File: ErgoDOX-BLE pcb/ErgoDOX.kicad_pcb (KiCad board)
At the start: 2 copper layers, 182.8 x 158.9 mm, 118 parts, among them J1 Conn_01x04, J2 Conn_01x02_Female, J3 Conn_01x02_Female, J4 Conn_01x02, J5 Conn_01x02, J6 6PIN, P1 USB_C_Plug_USB2.0, Q1 Q_NPN_BCE, SW0:10 SW0:3, SW0:11 SW0:2, SW0:12 SW0:1, SW0:7 SW0:6, SW0:8 SW0:5, SW0:9 SW0:4, SW1:10 SW1:3, SW1:11 SW1:2, SW1:12 SW1:1, SW1:13 SW1:0, SW1:9 SW1:4, SW2:10 SW2:3, SW2:11 SW2:2, SW2:12 SW2:1, SW2:13 SW2:0, SW2:7 SW2:6, SW2:8 SW2:5, SW2:9 SW2:4, SW3:10 SW3:3, SW3:11 SW3:2, SW3:12 SW3:1, SW3:13 SW3:0, SW3:8 SW3:5, SW3:9 SW3:4, SW4:10 SW4:3, SW4:11 SW4:2, SW4:12 SW4:1, SW4:13 SW4:0, SW4:7 SW4:6, SW4:8 SW4:5, SW4:9 SW4:4, SW5:10 SW5:3, SW5:11 SW5:2, SW5:12 SW5:1, SW5:13 SW5:0, SW5:7 SW5:6, SW5:8 SW5:5, SW5:9 SW5:4, U1 MCP23018, U3 C0720B001F

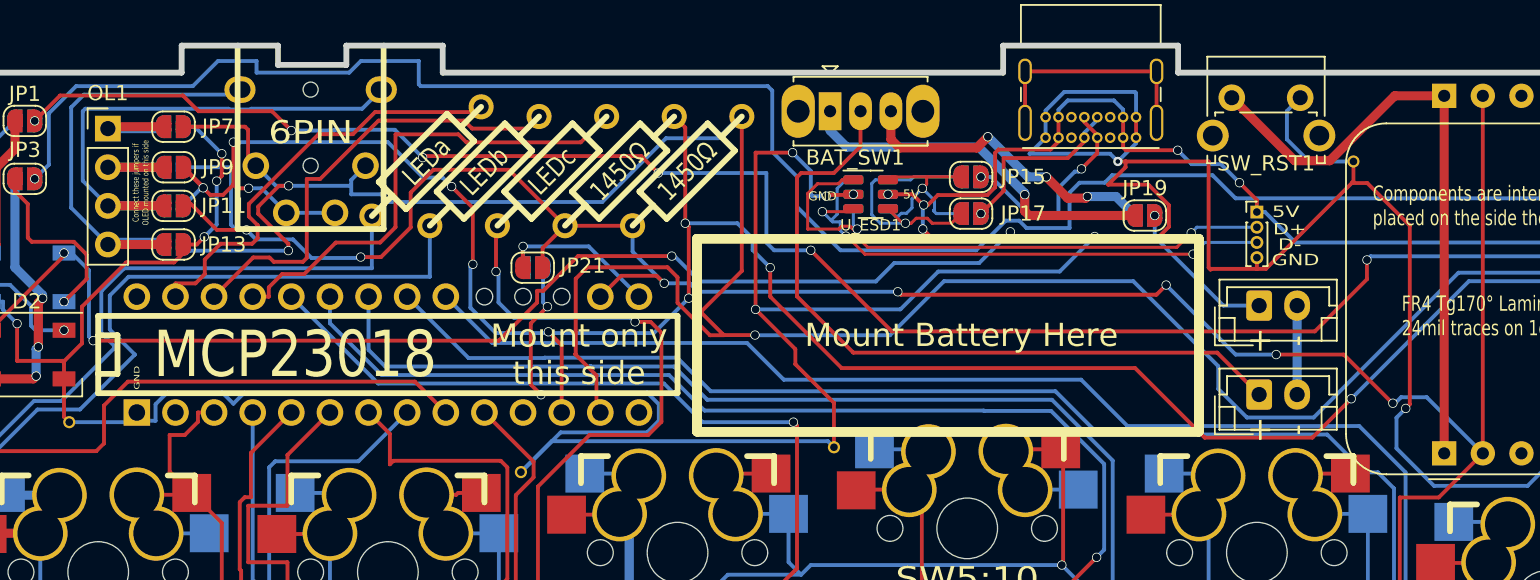
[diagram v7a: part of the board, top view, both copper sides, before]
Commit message: Begin playing around with replacing the 23018 with a 23017
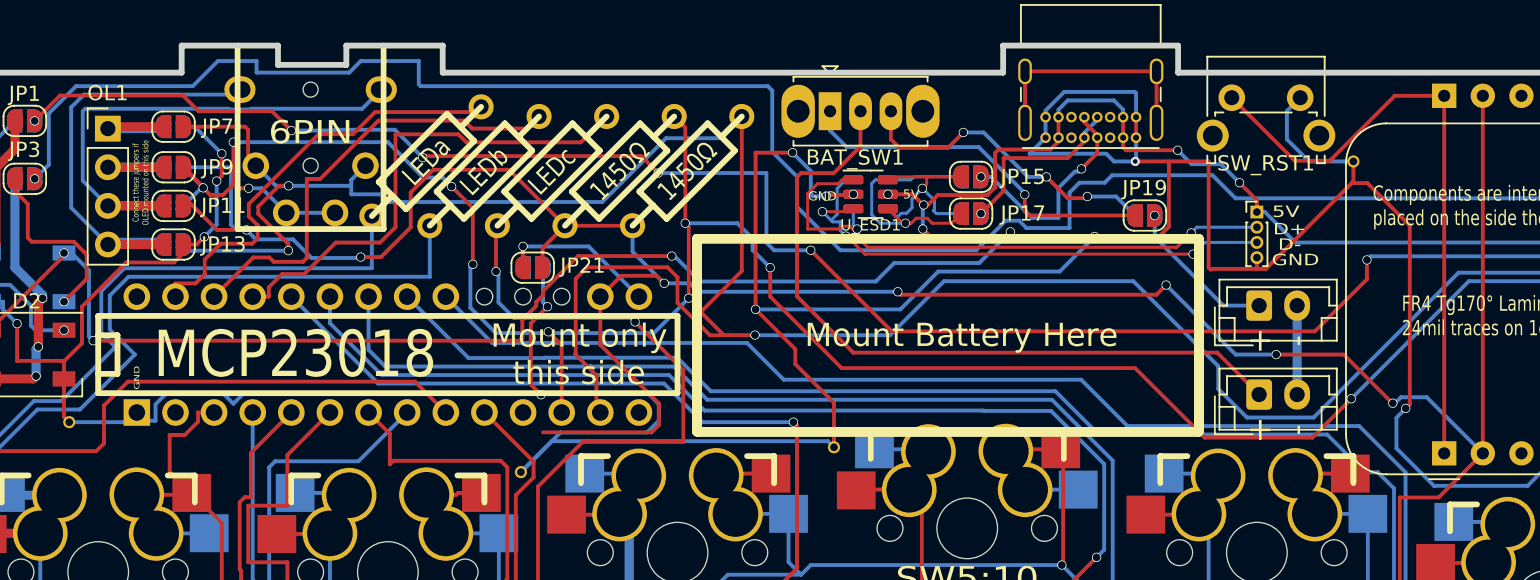
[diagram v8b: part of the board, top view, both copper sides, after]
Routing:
- net +3V3: track 316.4 -> 334.2 mm
- net GND: track 703.7 -> 699.5 mm
- net Net-(LED_C1-Pad1): track 111.9 -> 114.1 mm
- net +5V: track 181.1 -> 181.8 mm
